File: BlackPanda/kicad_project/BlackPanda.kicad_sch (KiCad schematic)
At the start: 86 parts, among them P1 TYPE-C-31-M-04, Q1 DDTA143ECA-7-F P08, Q2 DDTA143ECA-7-F P08, Q3 PDTC114EU, Q4 HY12P03C2, SW1 SW_Push, U1 AP22615AWU-7, U10 TJA1042TK-3, U11 TJA1042TK-3, U12 XL1509-3.3, U2 SiP32431DR3, U3 10_0_QHHTZB6_3, U4 NEO-M8M, U5 FM-B1921RGBA-SH, U6 TPS5450DDAR, U7 STM32F413RGTx, U8 TJA1042TK-3, U9 TJA1042TK-3, Y1 X322516MLB4SI

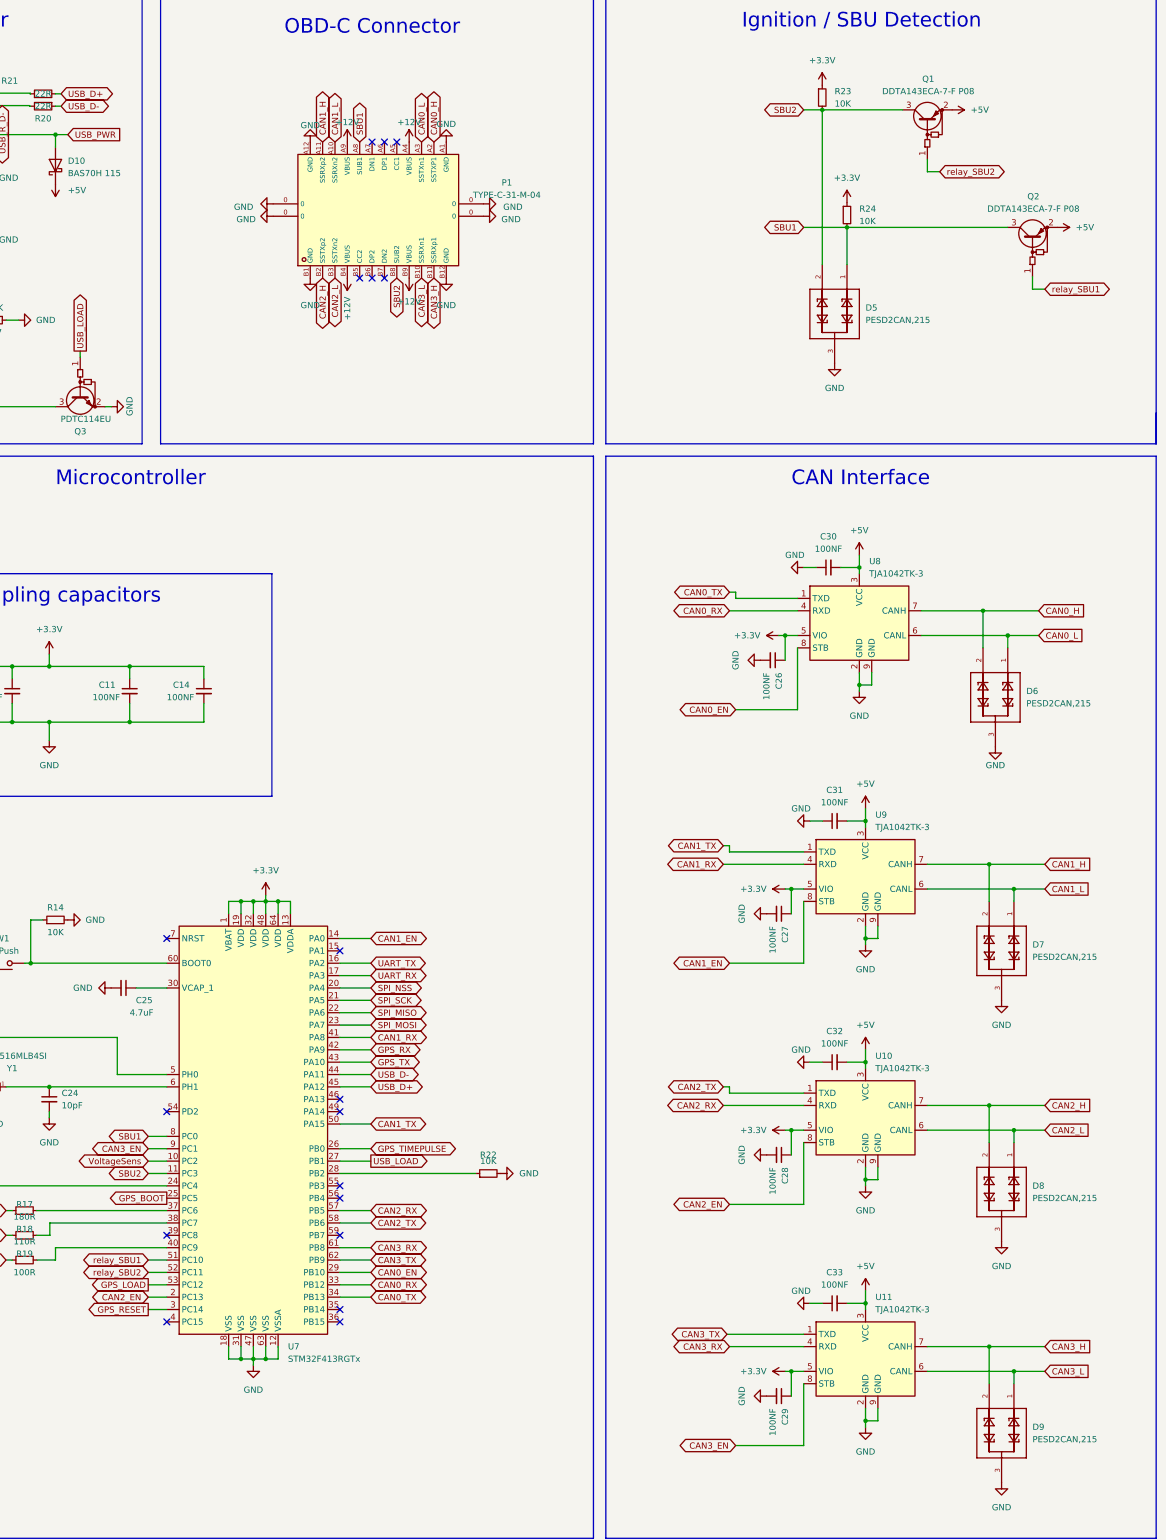
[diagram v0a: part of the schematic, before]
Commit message: CAN labels mirrored and rotated according to USB-C cables connections
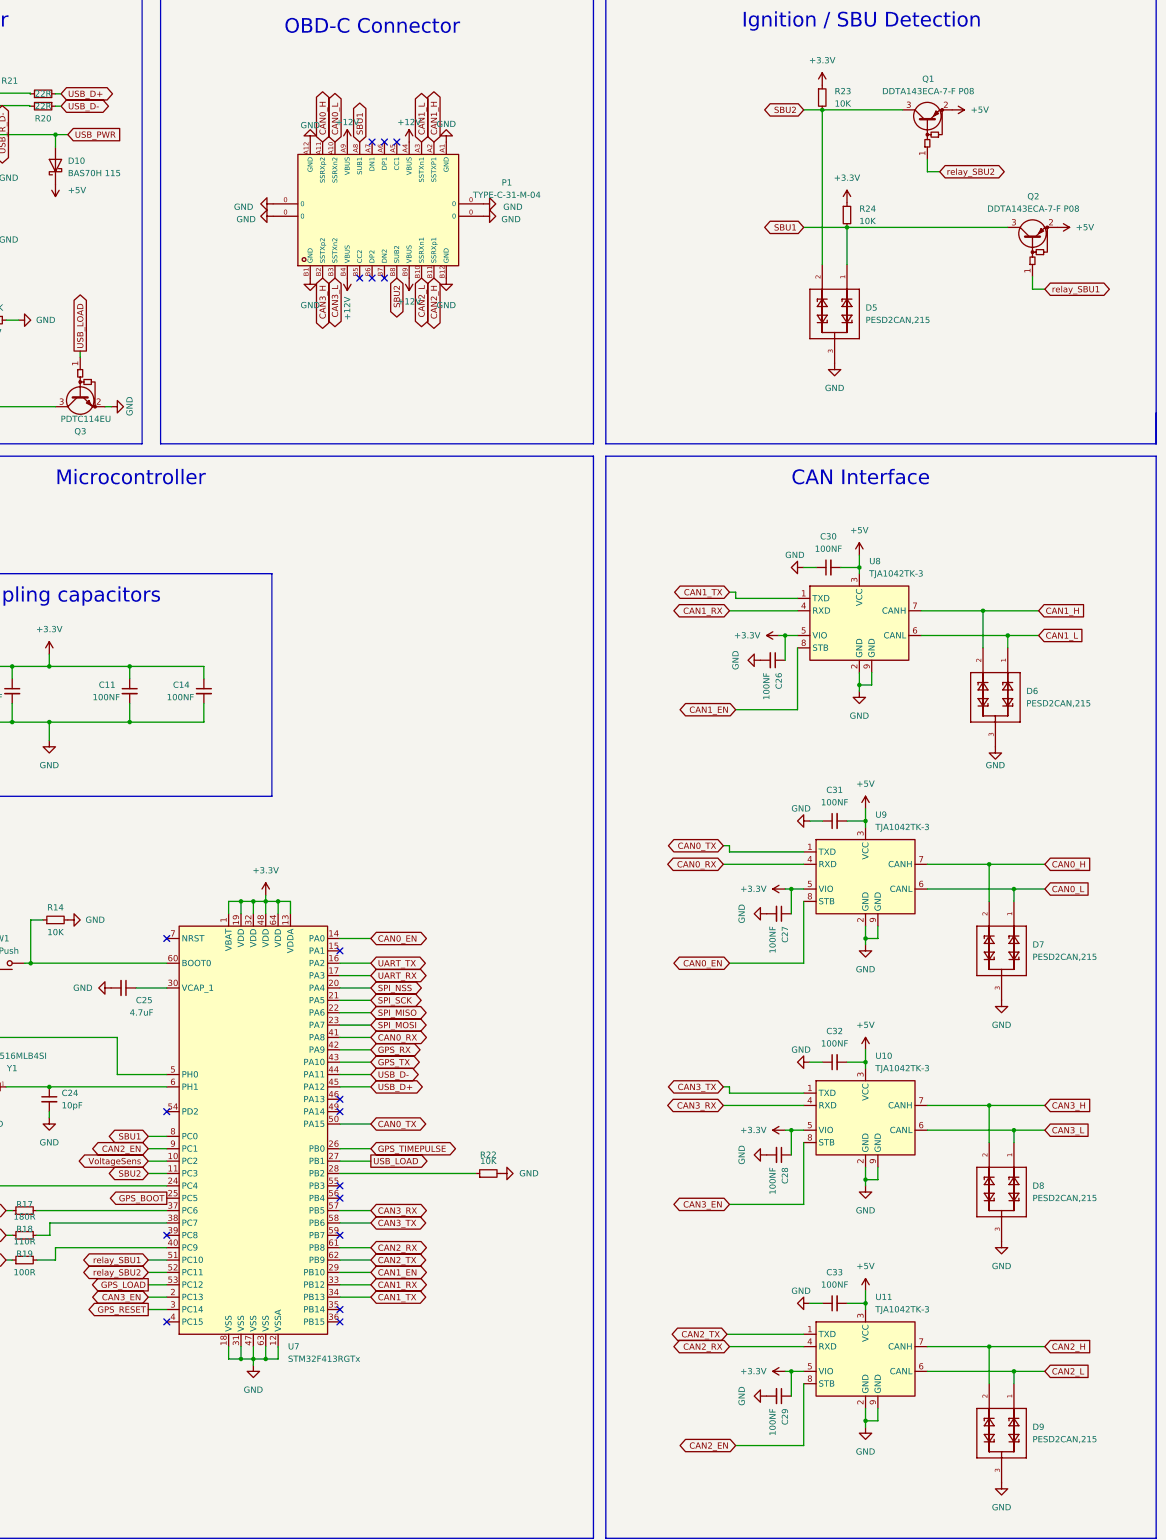
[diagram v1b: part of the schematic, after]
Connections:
- net CAN0_EN: now also U7.14 (PA0), U9.8 (STB); no longer U7.29 (PB10), U8.8 (STB)
- net CAN0_H: now also D7.2, P1.A11 (SSRXp2), U9.7 (CANH); no longer D6.2, P1.A2 (SSTXP1), U8.7 (CANH)
- net CAN0_L: now also D7.1, P1.A10 (SSRXn2), U9.6 (CANL); no longer D6.1, P1.A3 (SSTXn1), U8.6 (CANL)
- net CAN0_RX: now also U7.41 (PA8), U9.4 (RXD); no longer U7.33 (PB12), U8.4 (RXD)
- net CAN0_TX: now also U7.50 (PA15), U9.1 (TXD); no longer U7.34 (PB13), U8.1 (TXD)
- net CAN1_EN: now also U7.29 (PB10), U8.8 (STB); no longer U7.14 (PA0), U9.8 (STB)
- net CAN1_H: now also D6.2, P1.A2 (SSTXP1), U8.7 (CANH); no longer D7.2, P1.A11 (SSRXp2), U9.7 (CANH)
- net CAN1_L: now also D6.1, P1.A3 (SSTXn1), U8.6 (CANL); no longer D7.1, P1.A10 (SSRXn2), U9.6 (CANL)
- net CAN1_RX: now also U7.33 (PB12), U8.4 (RXD); no longer U7.41 (PA8), U9.4 (RXD)
- net CAN1_TX: now also U7.34 (PB13), U8.1 (TXD); no longer U7.50 (PA15), U9.1 (TXD)
- net CAN2_EN: now also U11.8 (STB), U7.9 (PC1); no longer U10.8 (STB), U7.2 (PC13)
- net CAN2_H: now also D9.2, P1.B11 (SSRXp1), U11.7 (CANH); no longer D8.2, P1.B2 (SSTXp2), U10.7 (CANH)
- net CAN2_L: now also D9.1, P1.B10 (SSRXn1), U11.6 (CANL); no longer D8.1, P1.B3 (SSTXn2), U10.6 (CANL)
- net CAN2_RX: now also U11.4 (RXD), U7.61 (PB8); no longer U10.4 (RXD), U7.57 (PB5)
- net CAN2_TX: now also U11.1 (TXD), U7.62 (PB9); no longer U10.1 (TXD), U7.58 (PB6)
- net CAN3_EN: now also U10.8 (STB), U7.2 (PC13); no longer U11.8 (STB), U7.9 (PC1)
- net CAN3_H: now also D8.2, P1.B2 (SSTXp2), U10.7 (CANH); no longer D9.2, P1.B11 (SSRXp1), U11.7 (CANH)
- net CAN3_L: now also D8.1, P1.B3 (SSTXn2), U10.6 (CANL); no longer D9.1, P1.B10 (SSRXn1), U11.6 (CANL)
- net CAN3_RX: now also U10.4 (RXD), U7.57 (PB5); no longer U11.4 (RXD), U7.61 (PB8)
- net CAN3_TX: now also U10.1 (TXD), U7.58 (PB6); no longer U11.1 (TXD), U7.62 (PB9)
